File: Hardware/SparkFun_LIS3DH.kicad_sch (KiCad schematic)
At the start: 29 parts, among them J1 Conn_01x02, J2 Conn_01x05, J3 Qwiic_RA, J4 I2C, J5 Qwiic_RA, U1 LIS3DH

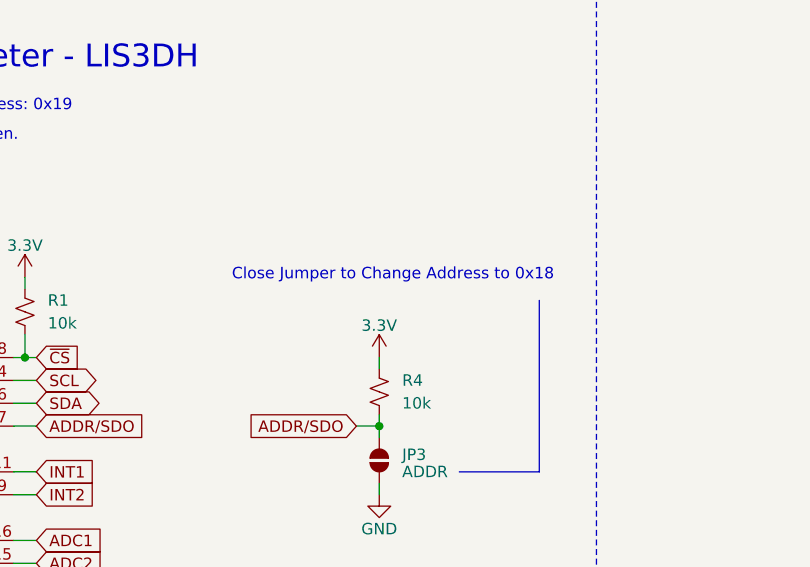
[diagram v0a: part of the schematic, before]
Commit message: Aligns the PTH for breadboard-ability
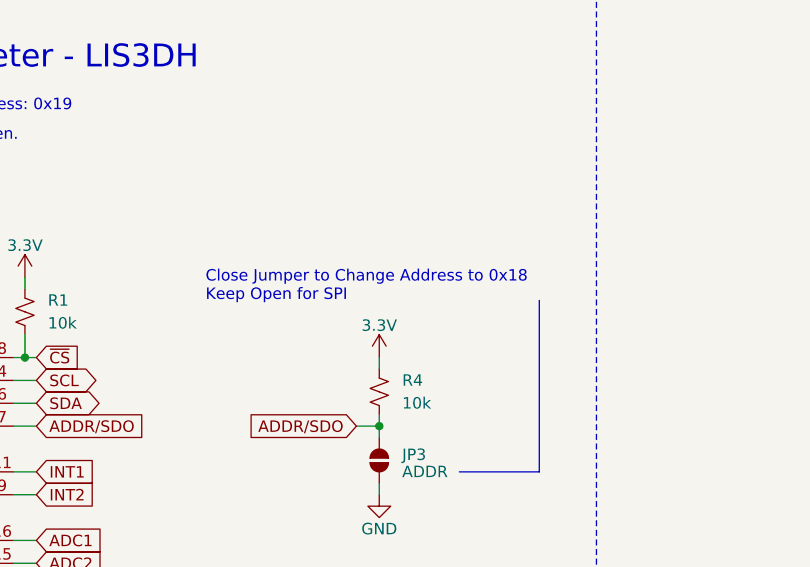
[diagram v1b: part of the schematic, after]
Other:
- note added: "Close Jumper to Change Address to 0x18 Keep Open for SPI"
- note removed: "Close Jumper to Change Address to 0x18"
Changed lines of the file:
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@@
 		)
 	)
-	(text "Close Jumper to Change Address to 0x18\n"
+	(text "Close Jumper to Change Address to 0x18\nKeep Open for SPI"
 		(exclude_from_sim no)
-		(at 136.144 49.276 0)
+		(at 115.316 50.546 0)
 		(effects
 			(font
 				(size 1.27 1.27)
 			)
+			(justify left)
 		)
 	)
